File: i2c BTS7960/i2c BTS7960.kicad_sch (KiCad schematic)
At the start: 38 parts, among them J1 power in, J6 to qwiic breakout, J7 qwiic 1, J8 qwiic 2, U12 ISO1540, U13 LD1117S33, U5 PCA9685, U90 mp1584 dcdc

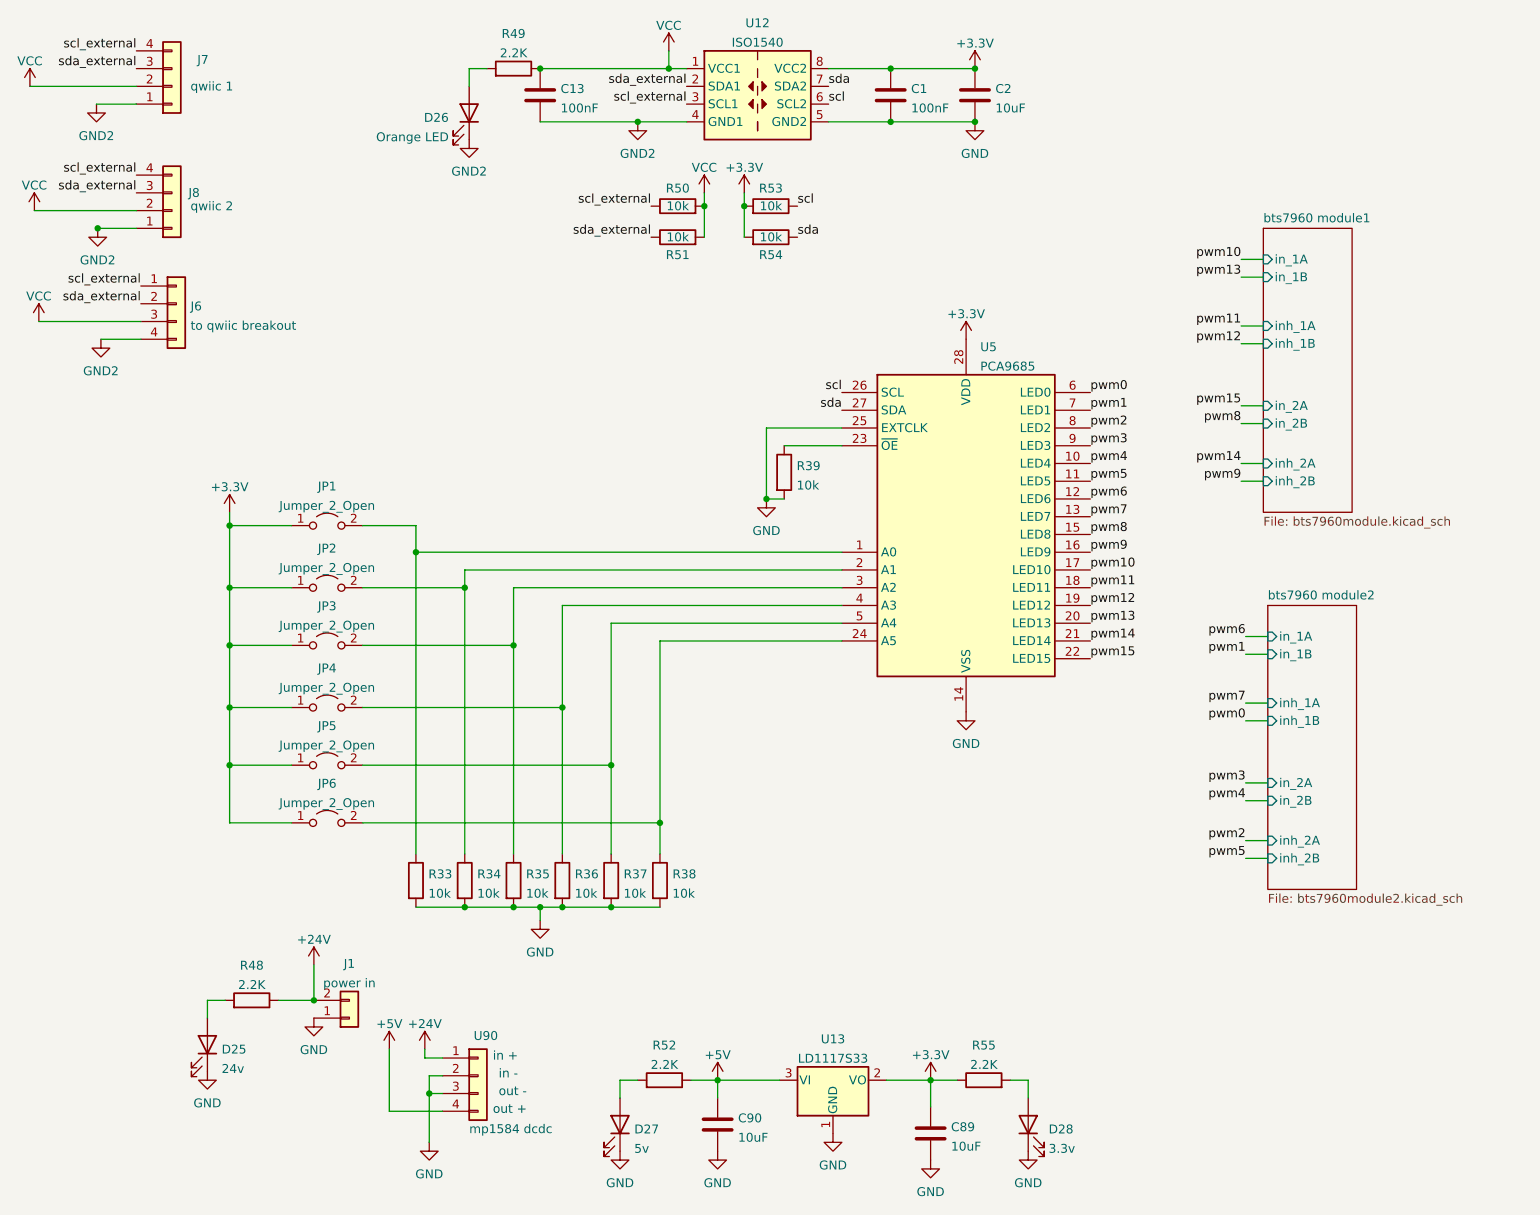
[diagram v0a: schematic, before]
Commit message: created scart TV breakout, revised motor controller and scale board for manufacturing
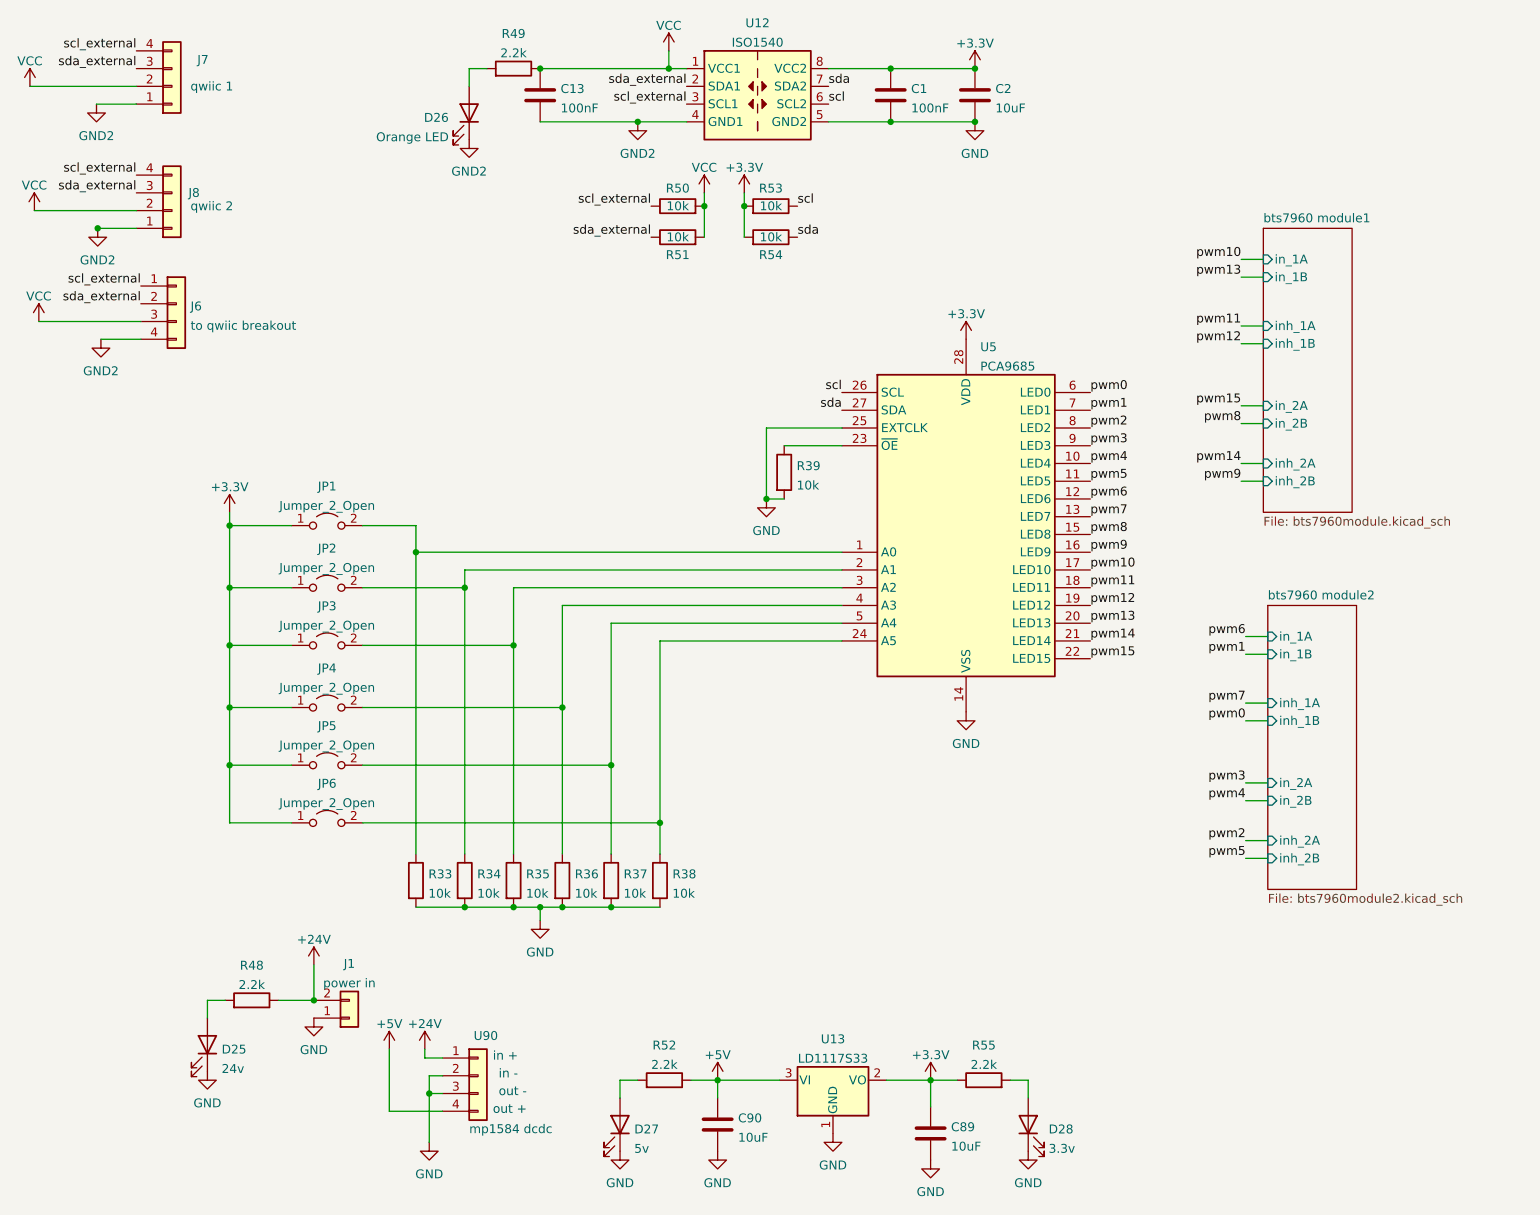
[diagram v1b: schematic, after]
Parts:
- R48, R49, R52, R55: value 2.2K -> 2.2k
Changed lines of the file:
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@@
     (in_bom yes) (on_board yes) (fields_autoplaced)
     (property "Reference" "R48" (id 0) (at 49.53 151.8625 90))
-    (property "Value" "2.2K" (id 1) (at 49.53 154.6376 90))
+    (property "Value" "2.2k" (id 1) (at 49.53 154.6376 90))
     (property "Footprint" "Resistor_SMD:R_0603_1608Metric" (id 2) (at 49.53 158.623 90)
       (effects (font (size 1.27 1.27)) hide)
@@
     (in_bom yes) (on_board yes) (fields_autoplaced)
     (property "Reference" "R49" (id 0) (at 86.995 18.5125 90))
-    (property "Value" "2.2K" (id 1) (at 86.995 21.2876 90))
+    (property "Value" "2.2k" (id 1) (at 86.995 21.2876 90))
     (property "Footprint" "Resistor_SMD:R_0603_1608Metric" (id 2) (at 86.995 25.273 90)
       (effects (font (size 1.27 1.27)) hide)
@@
     (in_bom yes) (on_board yes) (fields_autoplaced)
     (property "Reference" "R55" (id 0) (at 154.305 163.2925 90))
-    (property "Value" "2.2K" (id 1) (at 154.305 166.0676 90))
+    (property "Value" "2.2k" (id 1) (at 154.305 166.0676 90))
     (property "Footprint" "Resistor_SMD:R_0603_1608Metric" (id 2) (at 154.305 170.053 90)
       (effects (font (size 1.27 1.27)) hide)
@@
     (in_bom yes) (on_board yes) (fields_autoplaced)
     (property "Reference" "R52" (id 0) (at 108.585 163.2925 90))
-    (property "Value" "2.2K" (id 1) (at 108.585 166.0676 90))
+    (property "Value" "2.2k" (id 1) (at 108.585 166.0676 90))
     (property "Footprint" "Resistor_SMD:R_0603_1608Metric" (id 2) (at 108.585 170.053 90)
       (effects (font (size 1.27 1.27)) hide)
@@
     )
     (path "/0f7dd461-2f0d-4951-abf6-f2f24db77adb"
-      (reference "R48") (unit 1) (value "2.2K") (footprint "Resistor_SMD:R_0603_1608Metric")
+      (reference "R48") (unit 1) (value "2.2k") (footprint "Resistor_SMD:R_0603_1608Metric")
     )
     (path "/34ab7ed0-fca3-4b3d-8da0-8868d78a8add"
-      (reference "R49") (unit 1) (value "2.2K") (footprint "Resistor_SMD:R_0603_1608Metric")
+      (reference "R49") (unit 1) (value "2.2k") (footprint "Resistor_SMD:R_0603_1608Metric")
     )
     (path "/da29304b-fdb0-4932-a0f1-35b10e1f747d"
@@
     )
     (path "/d1bad49f-6fce-4a5c-802f-69e2bfe60a6a"
-      (reference "R52") (unit 1) (value "2.2K") (footprint "Resistor_SMD:R_0603_1608Metric")
+      (reference "R52") (unit 1) (value "2.2k") (footprint "Resistor_SMD:R_0603_1608Metric")
     )
     (path "/5b2d87e2-e6bb-49cc-9284-bd6d270146cd"
@@
     )
     (path "/6eeef786-33c2-4d11-9032-acda83b600f9"
-      (reference "R55") (unit 1) (value "2.2K") (footprint "Resistor_SMD:R_0603_1608Metric")
+      (reference "R55") (unit 1) (value "2.2k") (footprint "Resistor_SMD:R_0603_1608Metric")
     )
     (path "/861f5e51-ce87-4891-aa2b-840dfc68f4dc/10ac535c-8028-407d-9afd-71be4cdc3e79"

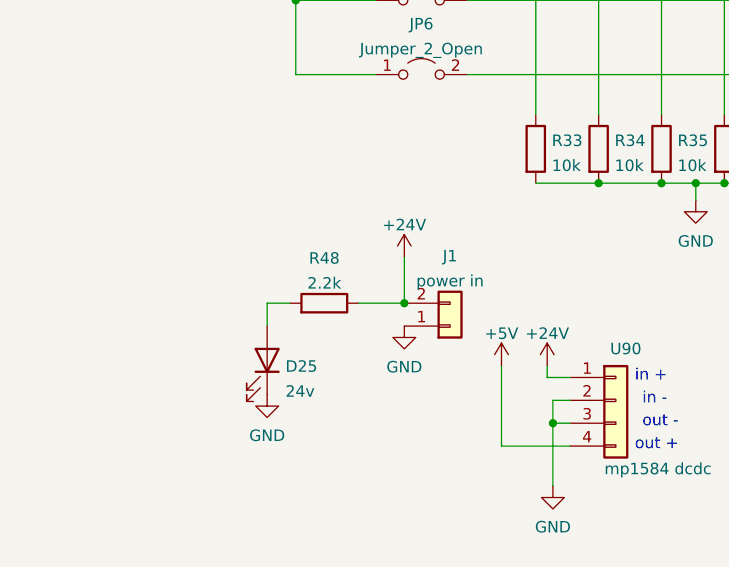
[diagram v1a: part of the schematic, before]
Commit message: tweaked buck converter hole sizes and silk
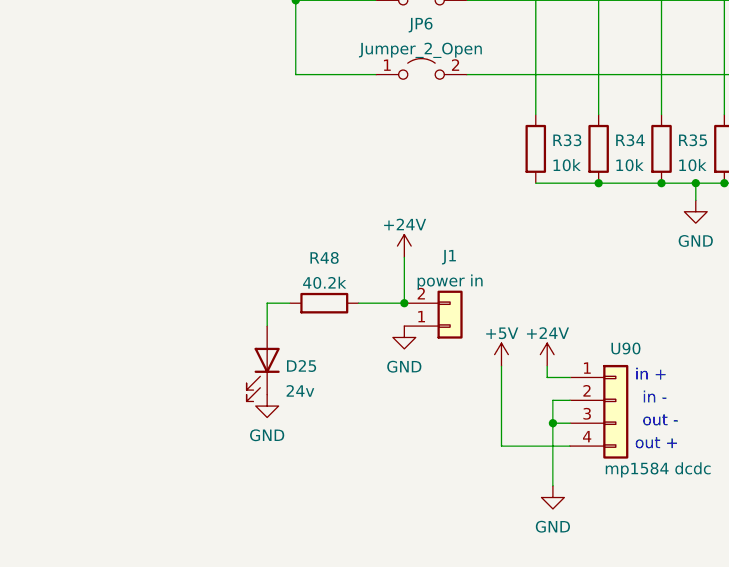
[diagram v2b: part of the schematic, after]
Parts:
- R48: value 2.2k -> 40.2k
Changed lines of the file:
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@@
     (in_bom yes) (on_board yes) (fields_autoplaced)
     (property "Reference" "R48" (id 0) (at 49.53 151.8625 90))
-    (property "Value" "2.2k" (id 1) (at 49.53 154.6376 90))
+    (property "Value" "40.2k" (id 1) (at 49.53 154.6376 90))
     (property "Footprint" "Resistor_SMD:R_0603_1608Metric" (id 2) (at 49.53 158.623 90)
       (effects (font (size 1.27 1.27)) hide)
@@
     )
     (path "/5bd48f92-7e14-495e-b0f0-e01697b3962a/bfdd4d05-52ad-4303-91b5-a03024fe25bf"
-      (reference "R17") (unit 1) (value "2.2k") (footprint "Resistor_SMD:R_0603_1608Metric")
+      (reference "R17") (unit 1) (value "10k") (footprint "Resistor_SMD:R_0603_1608Metric")
     )
     (path "/5bd48f92-7e14-495e-b0f0-e01697b3962a/e0a3b697-c6a1-4cbf-892c-3afd829a9665"
-      (reference "R18") (unit 1) (value "2.2k") (footprint "Resistor_SMD:R_0603_1608Metric")
+      (reference "R18") (unit 1) (value "10k") (footprint "Resistor_SMD:R_0603_1608Metric")
     )
     (path "/5bd48f92-7e14-495e-b0f0-e01697b3962a/7e77e9a9-832e-4b52-b7ce-33c895c49ebe"
-      (reference "R19") (unit 1) (value "2.2k") (footprint "Resistor_SMD:R_0603_1608Metric")
+      (reference "R19") (unit 1) (value "10k") (footprint "Resistor_SMD:R_0603_1608Metric")
     )
     (path "/5bd48f92-7e14-495e-b0f0-e01697b3962a/35d66f60-722c-4db2-9402-7035f3e93b72"
-      (reference "R20") (unit 1) (value "2.2k") (footprint "Resistor_SMD:R_0603_1608Metric")
+      (reference "R20") (unit 1) (value "10k") (footprint "Resistor_SMD:R_0603_1608Metric")
     )
     (path "/861f5e51-ce87-4891-aa2b-840dfc68f4dc/66a66c25-cca2-45d7-816b-22b904c47118"
@@
     )
     (path "/861f5e51-ce87-4891-aa2b-840dfc68f4dc/004ddc11-22fe-46d5-b5c2-3b2abd345029"
-      (reference "R31") (unit 1) (value "2.2k") (footprint "Resistor_SMD:R_0603_1608Metric")
+      (reference "R31") (unit 1) (value "10k") (footprint "Resistor_SMD:R_0603_1608Metric")
     )
     (path "/861f5e51-ce87-4891-aa2b-840dfc68f4dc/c38bf70b-e95c-4b21-9629-10d42640e9ea"
-      (reference "R32") (unit 1) (value "2.2k") (footprint "Resistor_SMD:R_0603_1608Metric")
+      (reference "R32") (unit 1) (value "10k") (footprint "Resistor_SMD:R_0603_1608Metric")
     )
     (path "/2e8dbda0-cfae-4f3f-8632-81c2c998844f"
@@
     )
     (path "/861f5e51-ce87-4891-aa2b-840dfc68f4dc/3ba95a31-8877-433d-ad16-d60e6f0d6ece"
-      (reference "R42") (unit 1) (value "2.2k") (footprint "Resistor_SMD:R_0603_1608Metric")
+      (reference "R42") (unit 1) (value "10k") (footprint "Resistor_SMD:R_0603_1608Metric")
     )
     (path "/861f5e51-ce87-4891-aa2b-840dfc68f4dc/20715fb4-3ed4-43b7-8ec8-b37bf7c05cce"
-      (reference "R43") (unit 1) (value "2.2k") (footprint "Resistor_SMD:R_0603_1608Metric")
+      (reference "R43") (unit 1) (value "10k") (footprint "Resistor_SMD:R_0603_1608Metric")
     )
     (path "/0f7dd461-2f0d-4951-abf6-f2f24db77adb"
-      (reference "R48") (unit 1) (value "2.2k") (footprint "Resistor_SMD:R_0603_1608Metric")
+      (reference "R48") (unit 1) (value "40.2k") (footprint "Resistor_SMD:R_0603_1608Metric")
     )
     (path "/34ab7ed0-fca3-4b3d-8da0-8868d78a8add"
